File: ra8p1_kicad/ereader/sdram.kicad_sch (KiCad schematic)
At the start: 14 parts, among them U14 IS42S32160F-7TLI

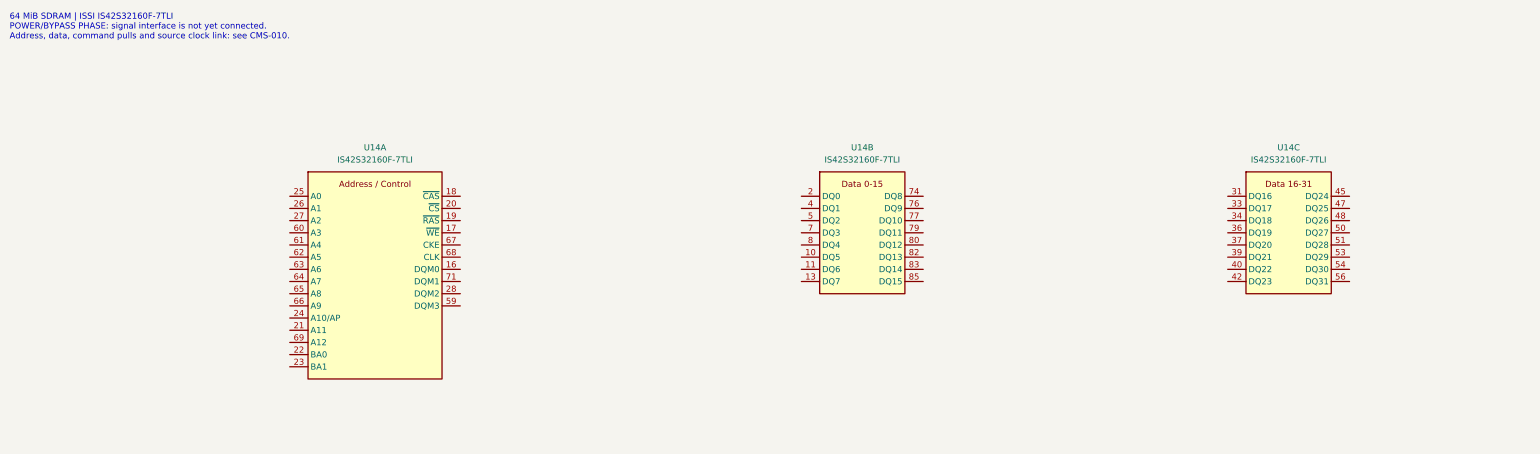
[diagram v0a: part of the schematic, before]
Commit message: Connect SDRAM signals through the schematic hierarchy
Wire the verified 57-signal RA8P1 interface and separate source/load clock nets through R43. Refresh the native BOM, linked CMS-010 contract, and complete ten-page PDF.

ERC: 139 prior findings resolved, zero new identities; 145 errors and two active warnings remain in the unfinished design. MCU pin-role typing, command pullups, and timing qualification remain open under #827.
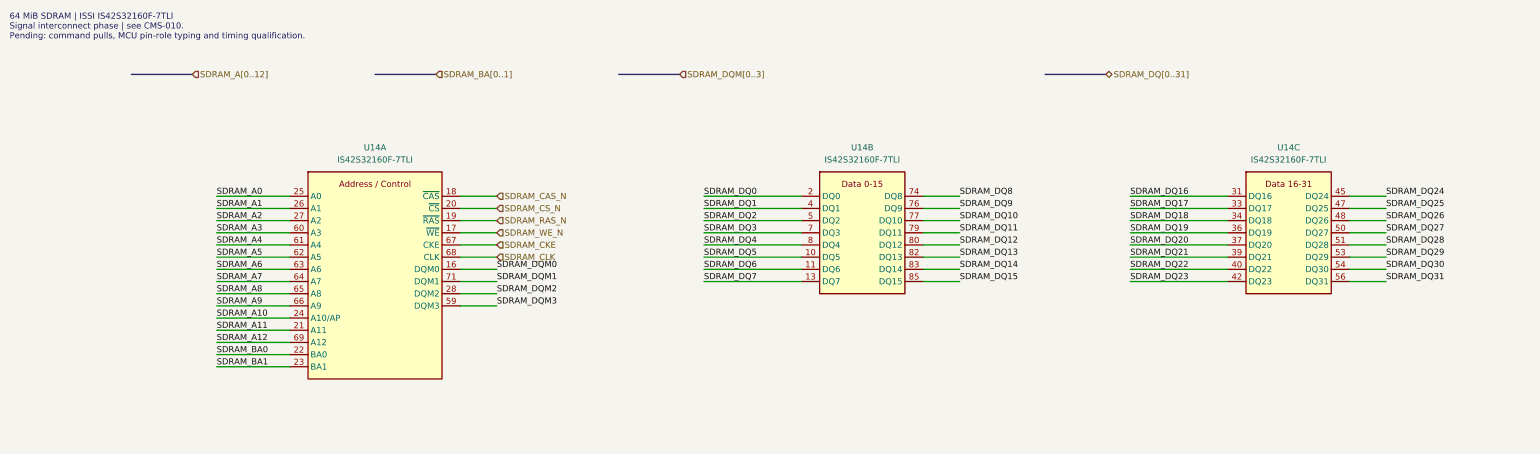
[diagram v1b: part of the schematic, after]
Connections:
- net SDRAM_DQM0: now reaches U14.16 (DQM0)
- net SDRAM_WE_N: now reaches U14.17 (~{WE})
- net SDRAM_CAS_N: now reaches U14.18 (~{CAS})
- net SDRAM_RAS_N: now reaches U14.19 (~{RAS})
- net SDRAM_CS_N: now reaches U14.20 (~{CS})
- net SDRAM_A11: now reaches U14.21 (A11)
- net SDRAM_BA0: now reaches U14.22 (BA0)
- net SDRAM_BA1: now reaches U14.23 (BA1)
- net SDRAM_A10: now reaches U14.24 (A10/AP)
- net SDRAM_A0: now reaches U14.25 (A0)
- net SDRAM_A1: now reaches U14.26 (A1)
- net SDRAM_A2: now reaches U14.27 (A2)
- net SDRAM_DQM2: now reaches U14.28 (DQM2)
- net SDRAM_DQM3: now reaches U14.59 (DQM3)
- net SDRAM_A3: now reaches U14.60 (A3)
- net SDRAM_A4: now reaches U14.61 (A4)
- net SDRAM_A5: now reaches U14.62 (A5)
- net SDRAM_A6: now reaches U14.63 (A6)
- net SDRAM_A7: now reaches U14.64 (A7)
- net SDRAM_A8: now reaches U14.65 (A8)
- net SDRAM_A9: now reaches U14.66 (A9)
- net SDRAM_CKE: now reaches U14.67 (CKE)
- net SDRAM_CLK: now reaches U14.68 (CLK)
- net SDRAM_A12: now reaches U14.69 (A12)
- net SDRAM_DQM1: now reaches U14.71 (DQM1)
- net SDRAM_DQ16: now reaches U14.31 (DQ16)
- net SDRAM_DQ17: now reaches U14.33 (DQ17)
- net SDRAM_DQ18: now reaches U14.34 (DQ18)
- net SDRAM_DQ19: now reaches U14.36 (DQ19)
- net SDRAM_DQ20: now reaches U14.37 (DQ20)
- net SDRAM_DQ21: now reaches U14.39 (DQ21)
- net SDRAM_DQ22: now reaches U14.40 (DQ22)
- net SDRAM_DQ23: now reaches U14.42 (DQ23)
- net SDRAM_DQ24: now reaches U14.45 (DQ24)
- net SDRAM_DQ25: now reaches U14.47 (DQ25)
- net SDRAM_DQ26: now reaches U14.48 (DQ26)
- net SDRAM_DQ27: now reaches U14.50 (DQ27)
- net SDRAM_DQ28: now reaches U14.51 (DQ28)
- net SDRAM_DQ29: now reaches U14.53 (DQ29)
- net SDRAM_DQ30: now reaches U14.54 (DQ30)
- net SDRAM_DQ31: now reaches U14.56 (DQ31)
- net SDRAM_DQ5: now reaches U14.10 (DQ5)
- net SDRAM_DQ6: now reaches U14.11 (DQ6)
- net SDRAM_DQ7: now reaches U14.13 (DQ7)
- net SDRAM_DQ0: now reaches U14.2 (DQ0)
- net SDRAM_DQ1: now reaches U14.4 (DQ1)
- net SDRAM_DQ2: now reaches U14.5 (DQ2)
- net SDRAM_DQ3: now reaches U14.7 (DQ3)
- net SDRAM_DQ8: now reaches U14.74 (DQ8)
- net SDRAM_DQ9: now reaches U14.76 (DQ9)
- net SDRAM_DQ10: now reaches U14.77 (DQ10)
- net SDRAM_DQ11: now reaches U14.79 (DQ11)
- net SDRAM_DQ4: now reaches U14.8 (DQ4)
- net SDRAM_DQ12: now reaches U14.80 (DQ12)
- net SDRAM_DQ13: now reaches U14.82 (DQ13)
- net SDRAM_DQ14: now reaches U14.83 (DQ14)
- net SDRAM_DQ15: now reaches U14.85 (DQ15)
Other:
- note added: "64 MiB SDRAM | ISSI IS42S32160F-7TLI Signal interconnect phase | see CMS-010. Pending: command pulls, MCU pin-role typing and timing qualification."
- note removed: "64 MiB SDRAM | ISSI IS42S32160F-7TLI POWER/BYPASS PHASE: signal interface is not yet connected. Address, data, command pulls and source clock link: see CMS-010."

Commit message: Add SDRAM reset defaults and MCU electrical pin roles
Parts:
- added R44, R45, R46, R47, R48, R49, R50, R51, R52, R53: 10k, symbol Device:R
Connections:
- net +3V3_MCU: now also R44.1, R45.1, R46.1, R47.1, R48.1, R49.1, R50.1, R51.1, R52.1, R53.1
- net SDRAM_CAS_N: now also R51.2
- net SDRAM_CKE: now also R44.2
- net SDRAM_CLK: now also R53.2
- net SDRAM_CS_N: now also R49.2
- net SDRAM_DQM0: now also R45.2
- net SDRAM_DQM1: now also R46.2
- net SDRAM_DQM2: now also R47.2
- net SDRAM_DQM3: now also R48.2
- net SDRAM_RAS_N: now also R50.2
- net SDRAM_WE_N: now also R52.2
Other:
- note added: "64 MiB SDRAM | ISSI IS42S32160F-7TLI Signal and reset-default circuits | CMS-010. Startup, SI/timing and hardware qualification remain open."
- note added: "CMS-010 | Pull load and power states Sink leakage: 5uA SDRAM+1uA board=6uA. Isink=3.6/9801+6uA=0.373309mA (<0.374mA). Pmax=3.6^2/9801=1.322314mW per pull. All ten LOW: 10*3.6/9801=3.673095mA rail; 10*3.6^2/9801=13.223140mW resistor heat. Reserve 4mA within the 250mA SDRAM allocation. CKE/DQM and CS_N default HIGH; CLK HIGH is not a clock. Switched-rail pulls; self-refresh actively holds CKE LOW. 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"
- note added: "CMS-010 | R44-R53: 10k reset defaults Rail 3.0..3.6V; +/-1%, 100ppm/C, |dT|<=100C. Rmin=10k*0.99*0.99=9801 ohm. Rmax=10k*1.01*1.01=10201 ohm. Ioff=5uA SDRAM+1uA MCU+1uA board=7uA. VHIGHmin=3.0-7uA*10201=2.928593V (>2.0V VIH). Board leakage and temperature screen require qualification."
- note removed: "64 MiB SDRAM | ISSI IS42S32160F-7TLI Signal interconnect phase | see CMS-010. Pending: command pulls, MCU pin-role typing and timing qualification."

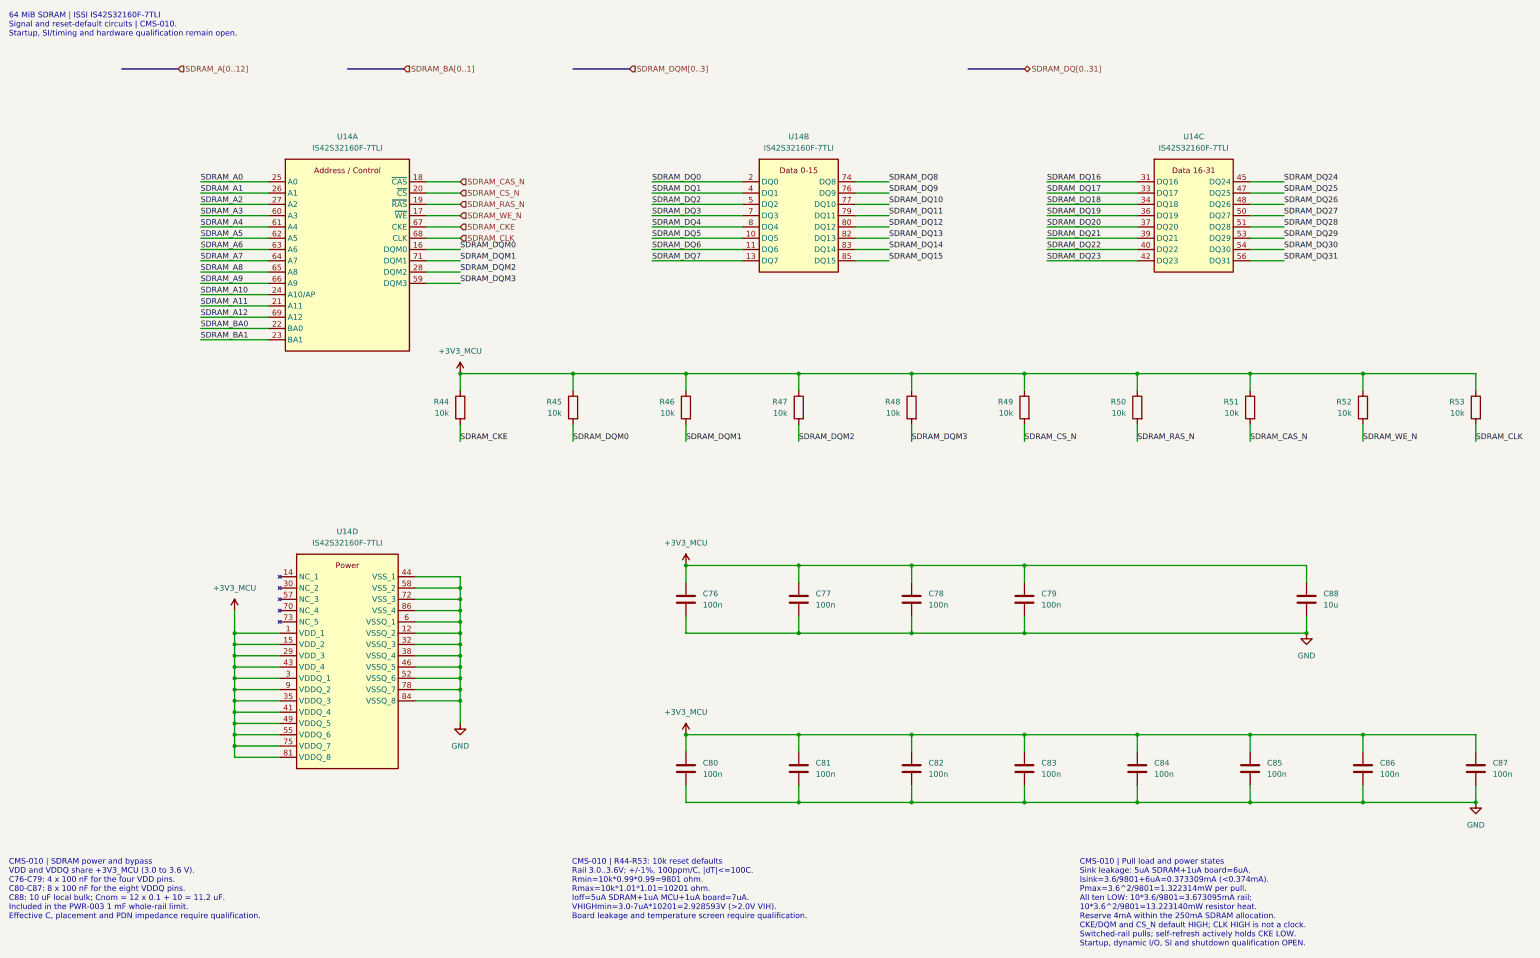
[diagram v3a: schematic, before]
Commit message: wip(hardware): preserve schematic cleanup and CEU host ports
Checkpoint cosmetic cleanup across the schematic hierarchy and eleven parallel-camera host ports. Refresh the complete 13-page PDF. All 334 existing net partitions and 271 component records match the prior CEU checkpoint; all 128 ERC identities remain unchanged. Electrical design is incomplete; this is a WIP checkpoint for #821 and #841.
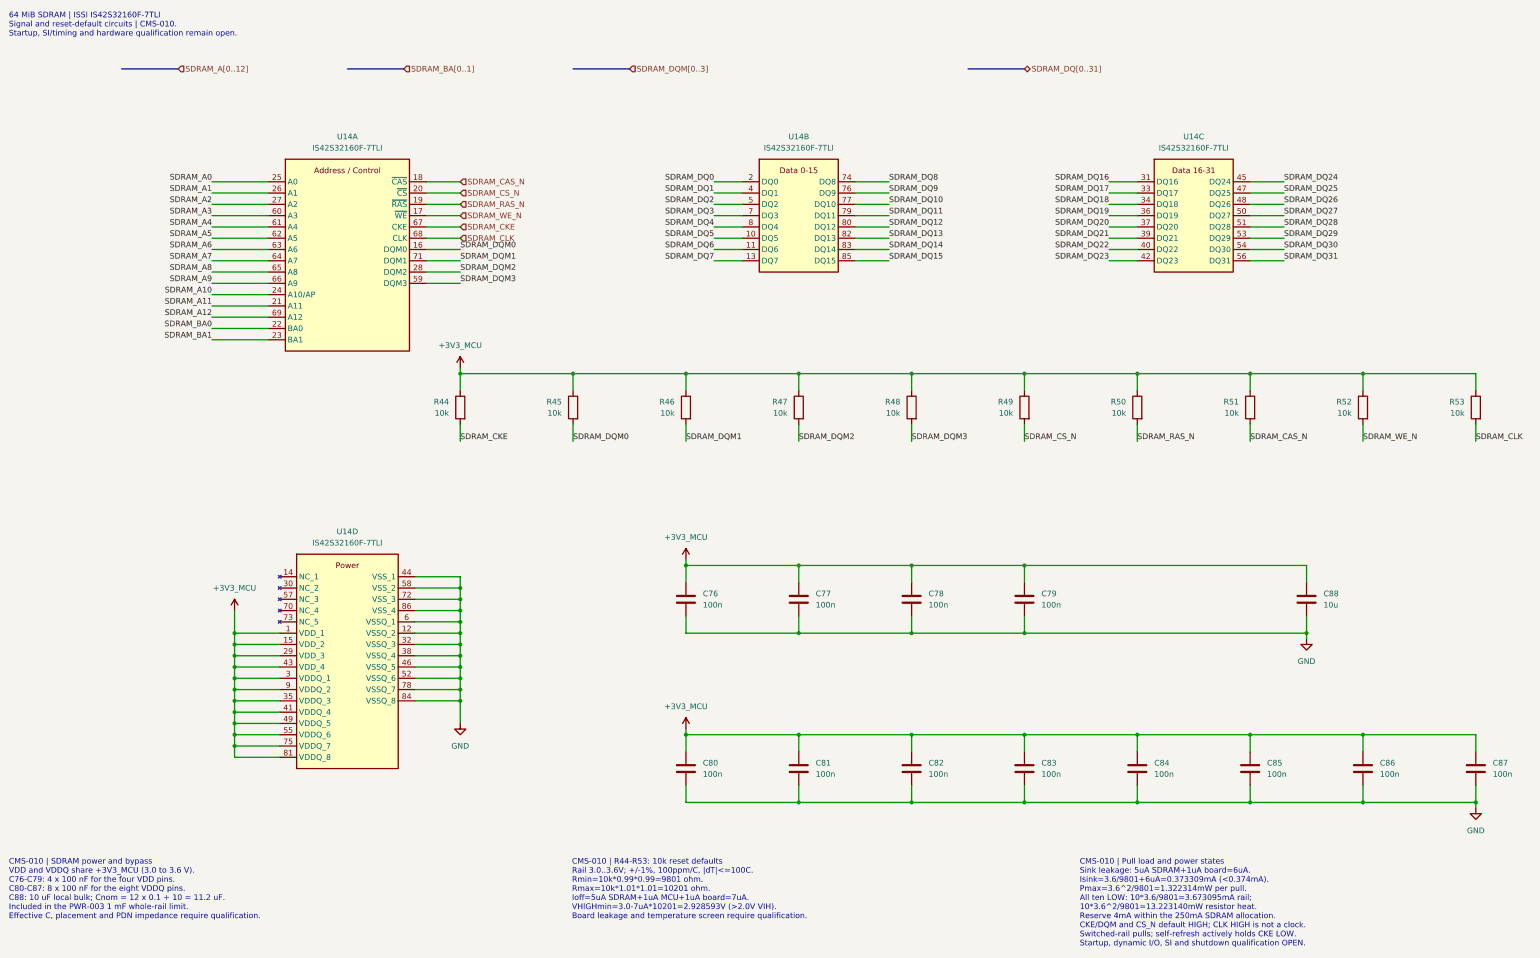
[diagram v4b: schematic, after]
